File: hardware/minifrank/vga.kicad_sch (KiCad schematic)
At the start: 9 parts, among them J10 VGA

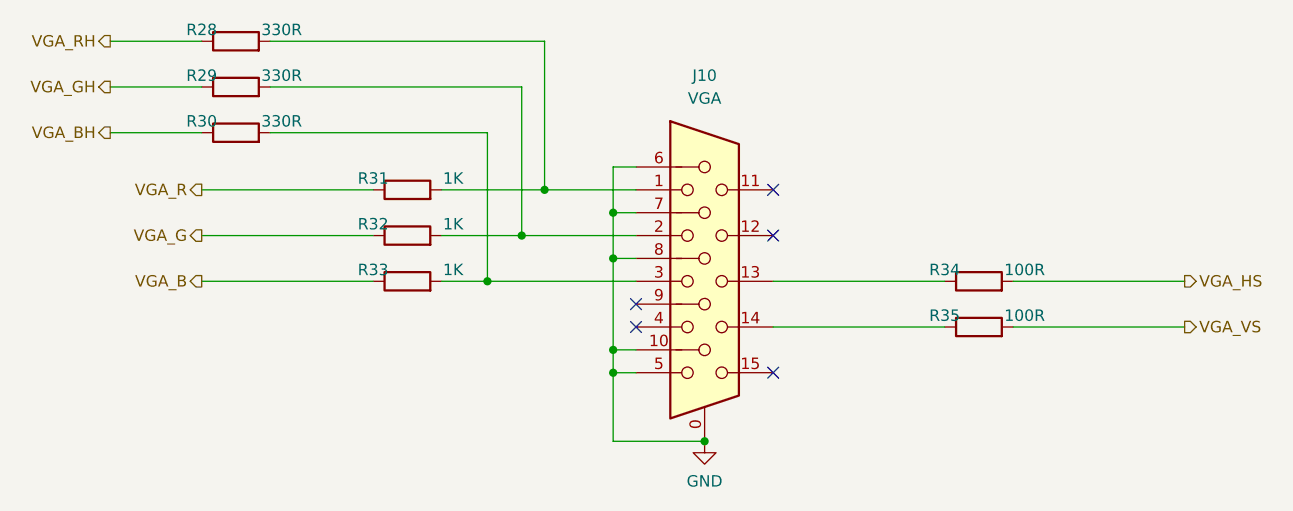
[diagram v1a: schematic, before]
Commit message: MiniFRANK: new board version
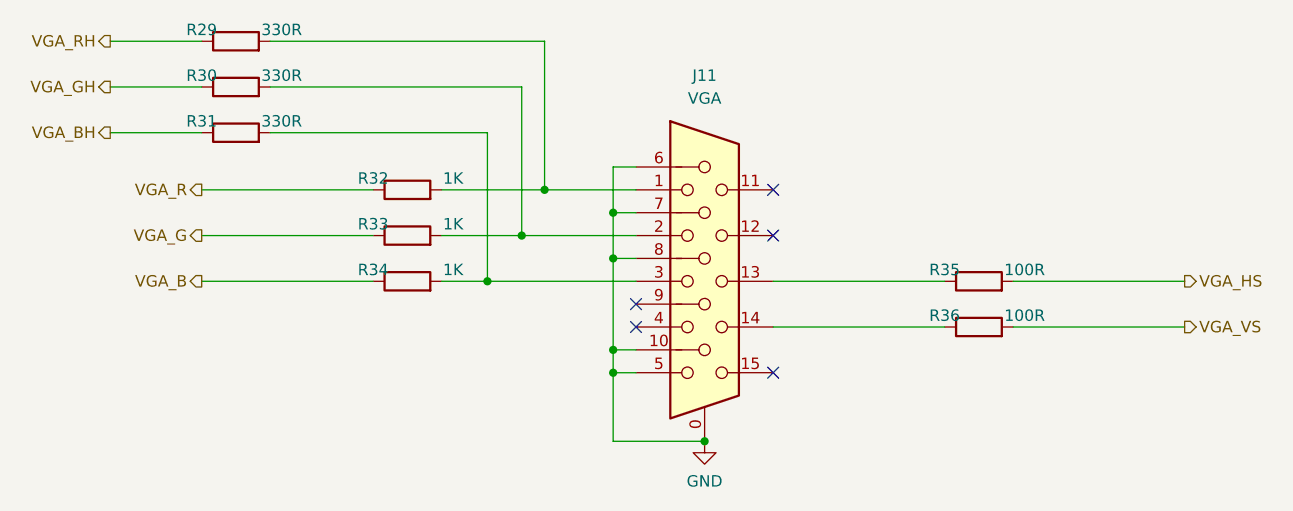
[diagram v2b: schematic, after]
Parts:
- J11: renamed from J10; footprint FRANK:D-SUB (15 pin, female) -> FRANK:DSUB-15_Female
- renumbered R28 to R29, R29 to R30, R30 to R31, R31 to R32, R32 to R33, R33 to R34, R34 to R35, R35 to R36
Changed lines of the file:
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@@
 		(in_pos_files yes)
 		(dnp no)
-		(property "Reference" "R30"
+		(property "Reference" "R31"
 			(at 101.6 85.09 90)
 			(show_name no)
@@
 			(project "minifrank"
 				(path "/8c0b3d8b-46d3-4173-ab1e-a61765f77d61/a290006b-7410-48d4-9859-f20399e5f780"
-					(reference "R30")
+					(reference "R31")
 					(unit 1)
 				)
@@
 		(in_pos_files yes)
 		(dnp no)
-		(property "Reference" "R35"
+		(property "Reference" "R36"
 			(at 184.15 106.68 90)
 			(show_name no)
@@
 			(project "minifrank"
 				(path "/8c0b3d8b-46d3-4173-ab1e-a61765f77d61/a290006b-7410-48d4-9859-f20399e5f780"
-					(reference "R35")
+					(reference "R36")
 					(unit 1)
 				)
@@
 		(dnp no)
 		(fields_autoplaced yes)
-		(property "Reference" "J10"
+		(property "Reference" "J11"
 			(at 157.48 80.01 0)
 			(show_name no)
@@
 			)
 		)
-		(property "Footprint" "FRANK:D-SUB (15 pin, female)"
+		(property "Footprint" "FRANK:DSUB-15_Female"
 			(at 133.35 92.71 0)
 			(hide yes)
@@
 			(project "minifrank"
 				(path "/8c0b3d8b-46d3-4173-ab1e-a61765f77d61/a290006b-7410-48d4-9859-f20399e5f780"
-					(reference "J10")
+					(reference "J11")
 					(unit 1)
 				)
@@
 		(in_pos_files yes)
 		(dnp no)
-		(property "Reference" "R32"
+		(property "Reference" "R33"
 			(at 120.65 96.52 90)
 			(show_name no)
@@
 			(project "minifrank"
 				(path "/8c0b3d8b-46d3-4173-ab1e-a61765f77d61/a290006b-7410-48d4-9859-f20399e5f780"
-					(reference "R32")
+					(reference "R33")
 					(unit 1)
 				)
@@
 		(dnp no)
 		(fields_autoplaced yes)
-		(property "Reference" "#PWR097"
+		(property "Reference" "#PWR0111"
 			(at 157.48 127 0)
 			(hide yes)
@@
 			(project "minifrank"
 				(path "/8c0b3d8b-46d3-4173-ab1e-a61765f77d61/a290006b-7410-48d4-9859-f20399e5f780"
-					(reference "#PWR097")
+					(reference "#PWR0111")
 					(unit 1)
 				)
@@
 		(in_pos_files yes)
 		(dnp no)
-		(property "Reference" "R31"
+		(property "Reference" "R32"
 			(at 120.65 91.44 90)
 			(show_name no)
@@
 			(project "minifrank"
 				(path "/8c0b3d8b-46d3-4173-ab1e-a61765f77d61/a290006b-7410-48d4-9859-f20399e5f780"
-					(reference "R31")
+					(reference "R32")
 					(unit 1)
 				)
@@
 		(in_pos_files yes)
 		(dnp no)
-		(property "Reference" "R34"
+		(property "Reference" "R35"
 			(at 184.15 101.6 90)
 			(show_name no)
@@
 			(project "minifrank"
 				(path "/8c0b3d8b-46d3-4173-ab1e-a61765f77d61/a290006b-7410-48d4-9859-f20399e5f780"
-					(reference "R34")
+					(reference "R35")
 					(unit 1)
 				)
@@
 		(in_pos_files yes)
 		(dnp no)
-		(property "Reference" "R29"
+		(property "Reference" "R30"
 			(at 101.6 80.01 90)
 			(show_name no)
@@
 			(project "minifrank"
 				(path "/8c0b3d8b-46d3-4173-ab1e-a61765f77d61/a290006b-7410-48d4-9859-f20399e5f780"
-					(reference "R29")
+					(reference "R30")
 					(unit 1)
 				)
@@
 		(in_pos_files yes)
 		(dnp no)
-		(property "Reference" "R28"
+		(property "Reference" "R29"
 			(at 101.6 74.93 90)
 			(show_name no)
@@
 			(project "minifrank"
 				(path "/8c0b3d8b-46d3-4173-ab1e-a61765f77d61/a290006b-7410-48d4-9859-f20399e5f780"
-					(reference "R28")
+					(reference "R29")
 					(unit 1)
 				)
@@
 		(in_pos_files yes)
 		(dnp no)
-		(property "Reference" "R33"
+		(property "Reference" "R34"
 			(at 120.65 101.6 90)
 			(show_name no)
@@
 			(project "minifrank"
 				(path "/8c0b3d8b-46d3-4173-ab1e-a61765f77d61/a290006b-7410-48d4-9859-f20399e5f780"
-					(reference "R33")
-					(unit 1)
-				)
+					(reference "R34")
+					(unit 1)
+				)
